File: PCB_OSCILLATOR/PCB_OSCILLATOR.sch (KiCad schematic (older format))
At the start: 99 parts, among them J1 Jumper, J10 Jumper, J11 Jumper, J12 Jumper, J13 Jumper, J14 Jumper, J15 Jumper, J16 Jumper, J2 Jumper, J3 Jumper, J4 Jumper, J5 Jumper, J6 Jumper, J7 Jumper, J8 Jumper, J9 Jumper, P1 POWER SUPPLY, P2 MCLK_EXTERNAL, P3 SPI_AD5270_1, P4 SPI_AD5270_2, P5 SPI_AD9833_1, P6 SPI_AD9833_2, U1 AD5270, U10 ADR291, U2 AD8421, U3 AD9833, U4 AD5270, U5 AD8421, U6 AD9833, U7 ADG819, U8 ADP3303, U9 AD8651

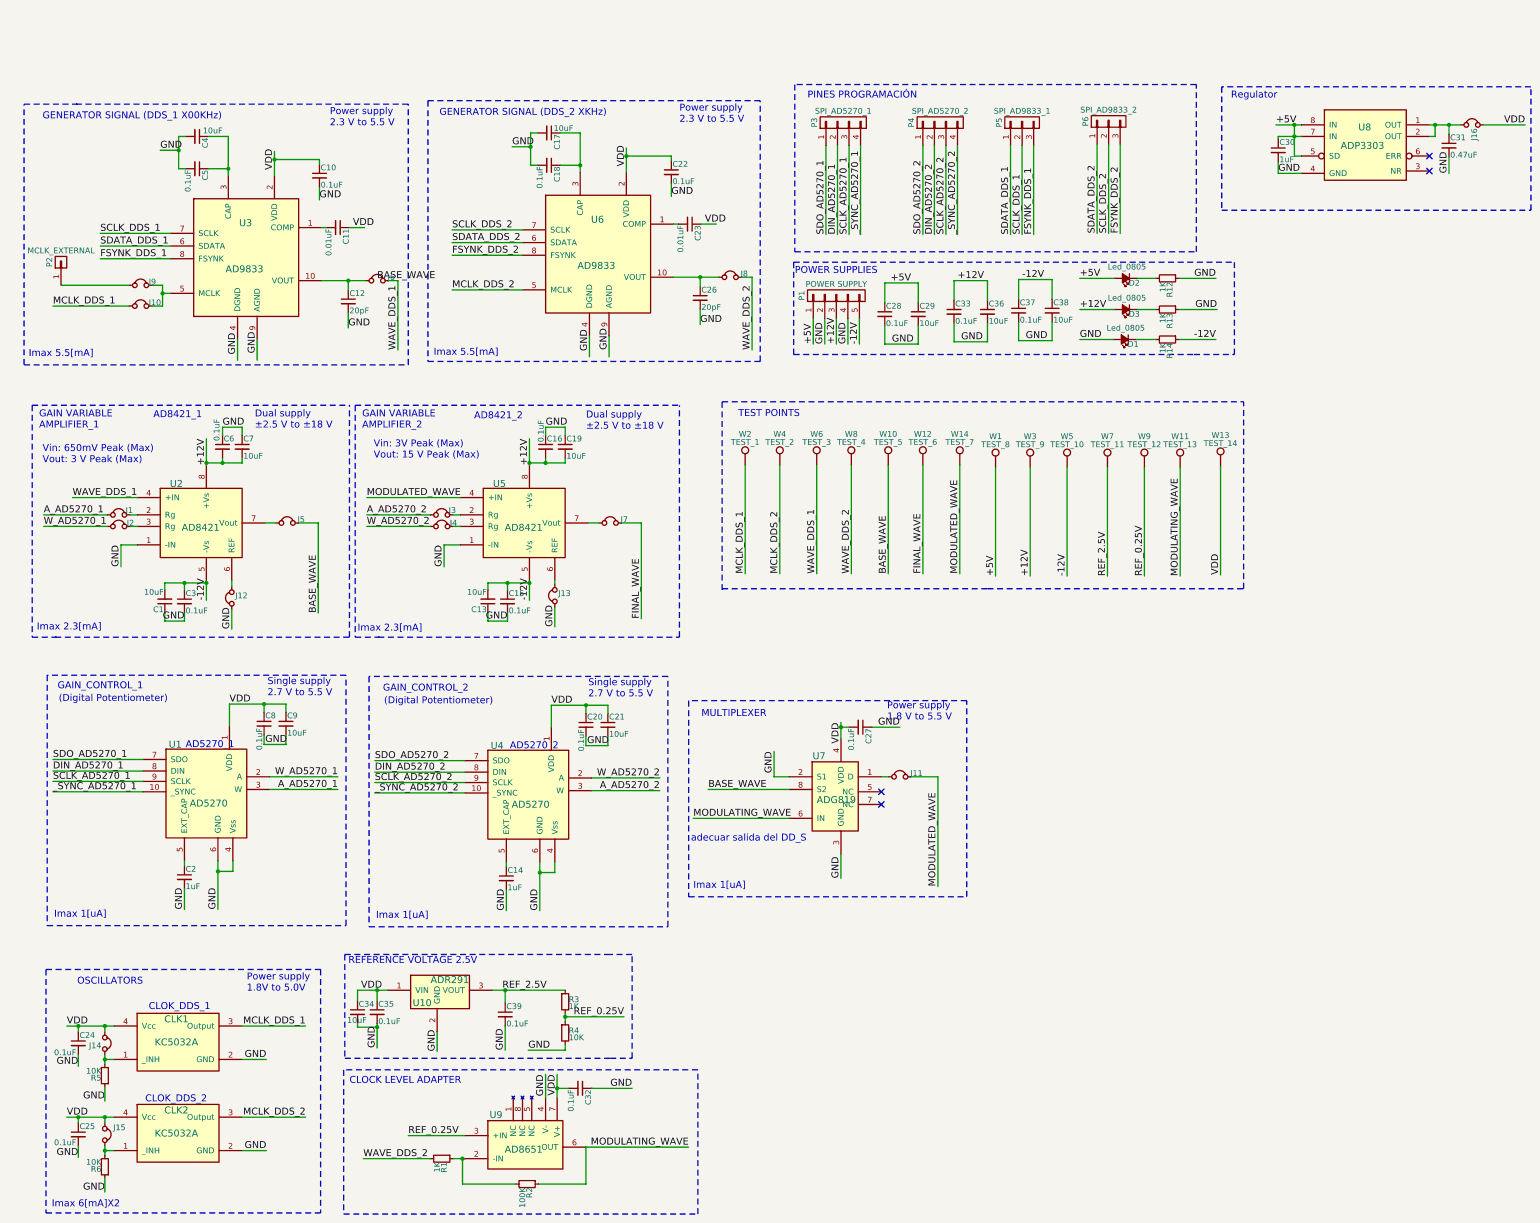
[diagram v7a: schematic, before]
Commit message: 80% PCB
Terminar conexiones de alimentación, regletas de +12 -12
y tratar de hacer el plano completo para tierra
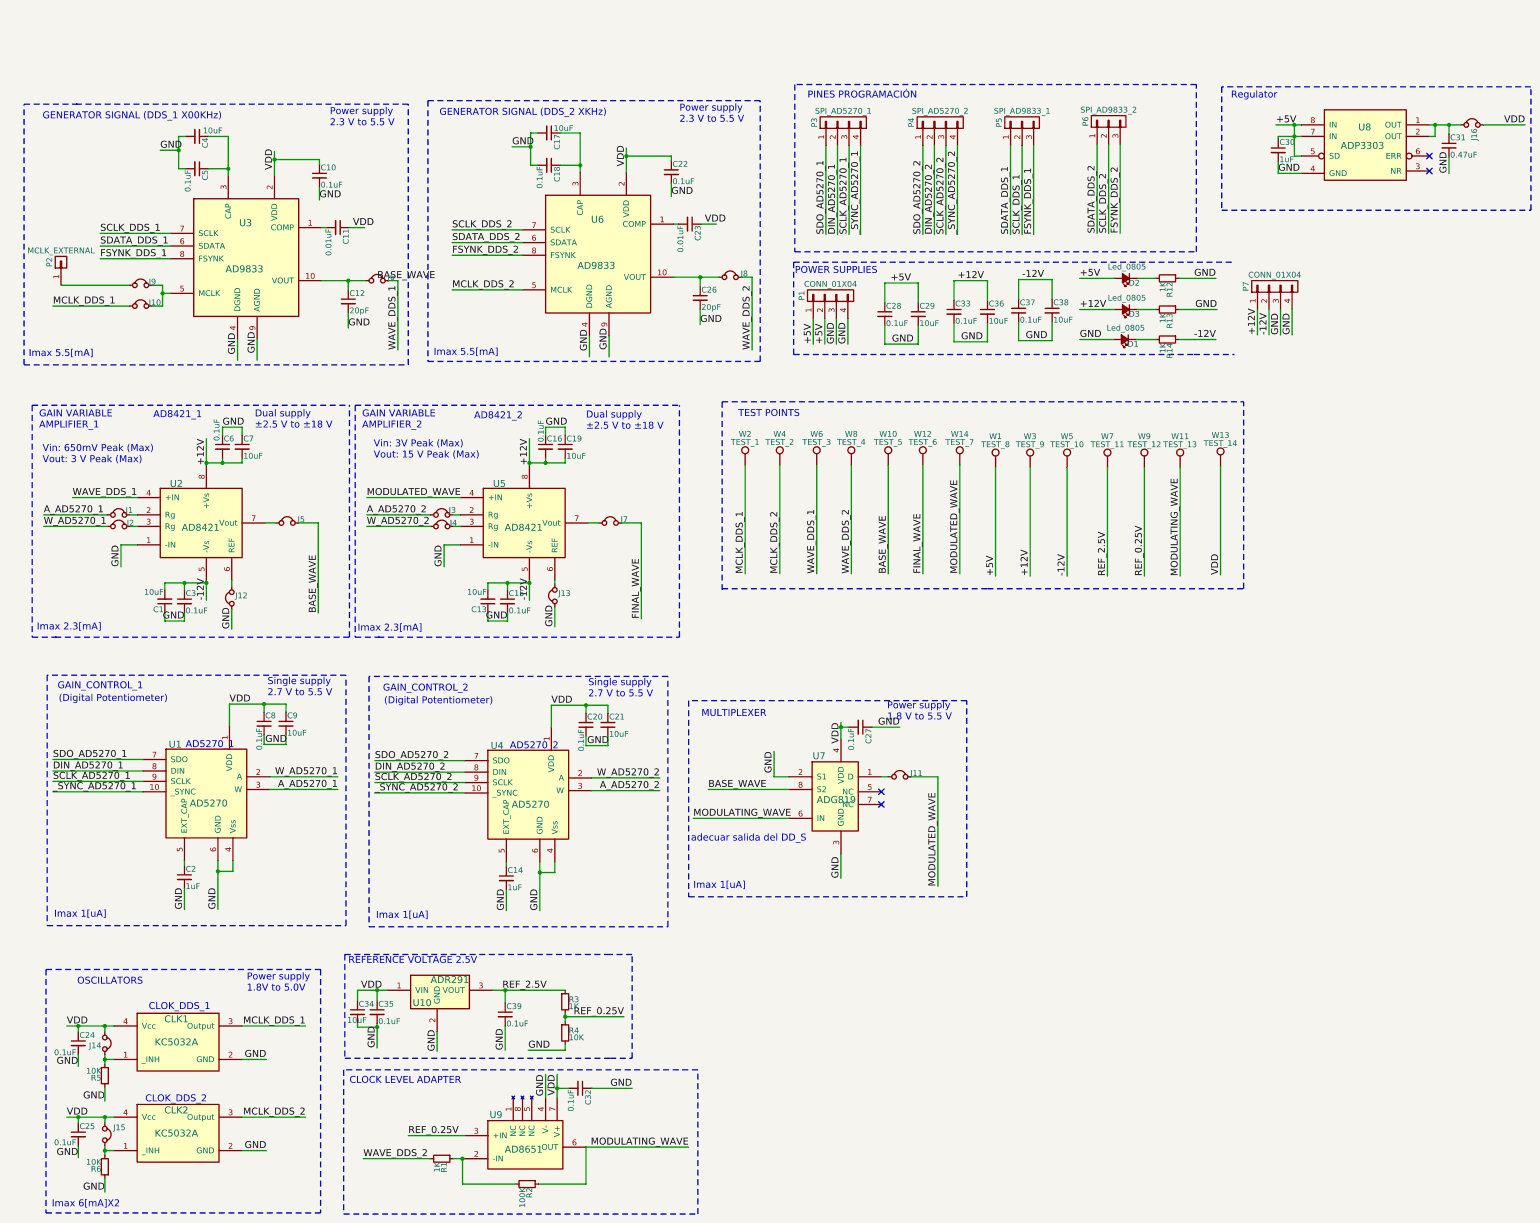
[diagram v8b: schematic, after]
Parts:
- removed P1: POWER SUPPLY, Socket_Strips:Socket_Strip_Straight_1x05, symbol CONN_01X05
- added P1, P7: CONN_01X04, Socket_Strips:Socket_Strip_Straight_1x04, symbol CONN_01X04
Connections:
- net +12V: now also P7.1 (P1)
- net +5V: now also P1.1 (P1), P1.2 (P2)
- net -12V: now also P7.2 (P2)
- net GND: now also P1.3 (P3), P1.4 (P4), P7.3 (P3), P7.4 (P4)
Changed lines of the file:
@@
 Text Label 7650 2940 1    60   ~ 0
 +5V
-Text Label 7750 2940 1    60   ~ 0
+Text Label 7850 2940 1    60   ~ 0
 GND
-$Comp
-L CONN_01X05 P1
-U 1 1 59168240
-P 7850 2520
-F 0 "P1" H 7850 2820 50  0000 C CNN
-F 1 "POWER SUPPLY" V 7950 2520 50  0000 C CNN
-F 2 "Socket_Strips:Socket_Strip_Straight_1x05" H 7850 2520 50  0001 C CNN
-F 3 "" H 7850 2520 50  0000 C CNN
-	1    7850 2520
-	0    -1   -1   0
-$EndComp
-Text Label 7850 2940 1    60   ~ 0
+Text Label 11500 2860 1    60   ~ 0
 +12V
-Text Label 7950 2940 1    60   ~ 0
+Text Label 11700 2860 1    60   ~ 0
 GND
-Text Label 8050 2940 1    60   ~ 0
+Text Label 11600 2860 1    60   ~ 0
 -12V
 Text Label 6160 5320 1    60   ~ 0
@@
 	7650 2720 7650 2940
 Wire Wire Line
+	11500 2640 11500 2860
+Wire Wire Line
 	7850 2720 7850 2940
 Wire Wire Line
-	7750 2720 7750 2940
-Wire Wire Line
-	7950 2720 7950 2940
-Wire Wire Line
-	8050 2720 8050 2940
+	11700 2640 11700 2860
+Wire Wire Line
+	11600 2640 11600 2860
 Wire Wire Line
 	6160 4490 6160 5320
@@
 	4140 9800 4630 9800
 Wire Wire Line
-	4630 10000 4530 10000
+	4530 10000 4630 10000
 Wire Wire Line
 	3750 10000 4330 10000
@@
 	5500 9060 5180 9060
 Wire Wire Line
-	5500 8810 5500 8740
+	5500 8740 5500 8810
 Wire Wire Line
 	5500 8770 6010 8770
@@
 Wire Notes Line
 	10950 3030 11300 3030
-Wire Notes Line
-	11300 3030 11300 2230
 $Comp
 L 1K R3
@@
 Text Label 6740 6800 0    60   ~ 0
 BASE_WAVE
+$Comp
+L CONN_01X04 P1
+U 1 1 5919FAF3
+P 7800 2520
+F 0 "P1" H 7800 2770 50  0000 C CNN
+F 1 "CONN_01X04" V 7900 2520 50  0000 C CNN
+F 2 "Socket_Strips:Socket_Strip_Straight_1x04" H 7800 2520 50  0001 C CNN
+F 3 "" H 7800 2520 50  0000 C CNN
+	1    7800 2520
+	0    -1   -1   0
+$EndComp
+Text Label 7950 2940 1    60   ~ 0
+GND
+Wire Wire Line
+	7950 2720 7950 2940
+Text Label 7750 2940 1    60   ~ 0
++5V
+Wire Wire Line
+	7750 2720 7750 2940
+$Comp
+L CONN_01X04 P7
+U 1 1 591A1F24
+P 11650 2440
+F 0 "P7" H 11650 2690 50  0000 C CNN
+F 1 "CONN_01X04" V 11750 2440 50  0000 C CNN
+F 2 "Socket_Strips:Socket_Strip_Straight_1x04" H 11650 2440 50  0001 C CNN
+F 3 "" H 11650 2440 50  0000 C CNN
+	1    11650 2440
+	0    -1   -1   0
+$EndComp
+Text Label 11800 2860 1    60   ~ 0
+GND
+Wire Wire Line
+	11800 2640 11800 2860
 $EndSCHEMATC
